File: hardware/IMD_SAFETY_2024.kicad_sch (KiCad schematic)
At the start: 94 parts, among them J1 Main- M80-5300842, K2 TE AXICOM IM07DTS, Q1 2N7002, Q2 2N7002, SW1 Push Button, U1 LM393, U10 74HCS08, U13 74HC74, U14 LM393, U15 LM393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

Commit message: OxDRC state, 2.1.0 ready to review, change connector to vertical, and R-Reset node slightly
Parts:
- J1: value Main- M80-5300842 -> Main- M80-5000842; footprint Samacsys:M80-53008YY -> footprints:M80-50008YY_2
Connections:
- net RESET: now also C13.1, D8.1 (A1), R22.1, U13.3 (C); no longer J1.4 (Pin_4), R22.2, SW1.2
- new net EXT_RESET: J1.4 (Pin_4), R22.2, SW1.2
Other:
- note added: "'0' WHEN > 3.27V ON RISING OF PWM"
- note added: "Legacy RC Hold, populate only if necessary, otherwise short."
- note removed: "'0' WHEN > 1V ON RISING OF PWM"
- note removed: "DODAĆ TVS, CAP 100nF i 100R"
- note removed: "Jumper option"
- note removed: "Legacy RC Hold, bypass. populate only if necessary"
- moved on the sheet: D1, D3, Q2, R21, SW1

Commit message: 2.1.0 Release, adjust after review
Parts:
- added C22: 100nF, Capacitor_SMD:C_0603_1608Metric, symbol Device:C_Small
- F1: symbol PUTM_EV_IMD_SAFETY_2021-rescue:Fuse-Device -> Device:Polyfuse; Mouser# 667-ERB-RG0R50V -> 576-1206L050/24WR
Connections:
- net +12V: now also C22.1
- net GND: now also C22.2
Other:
- moved on the sheet: C4, C5

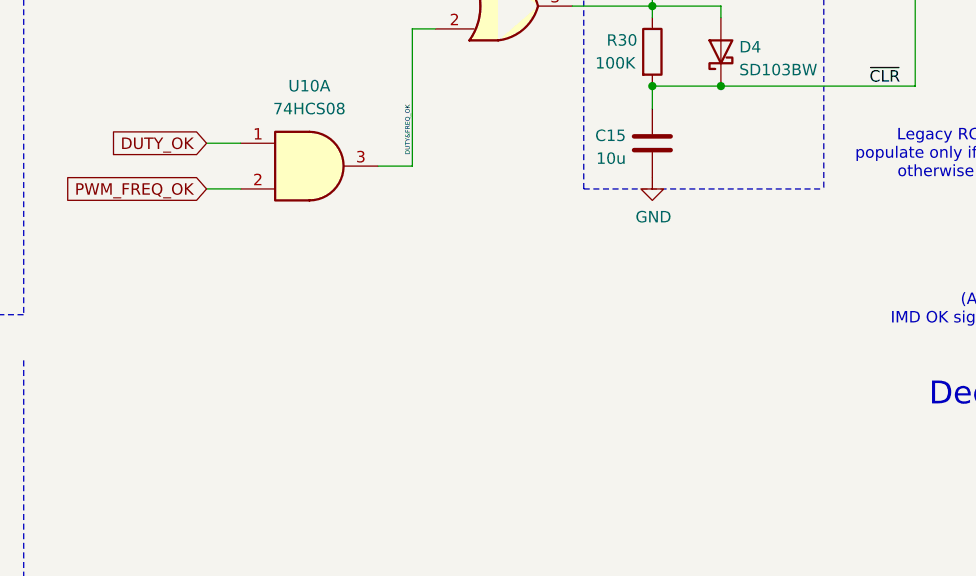
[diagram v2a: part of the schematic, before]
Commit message: Add 0V jumper
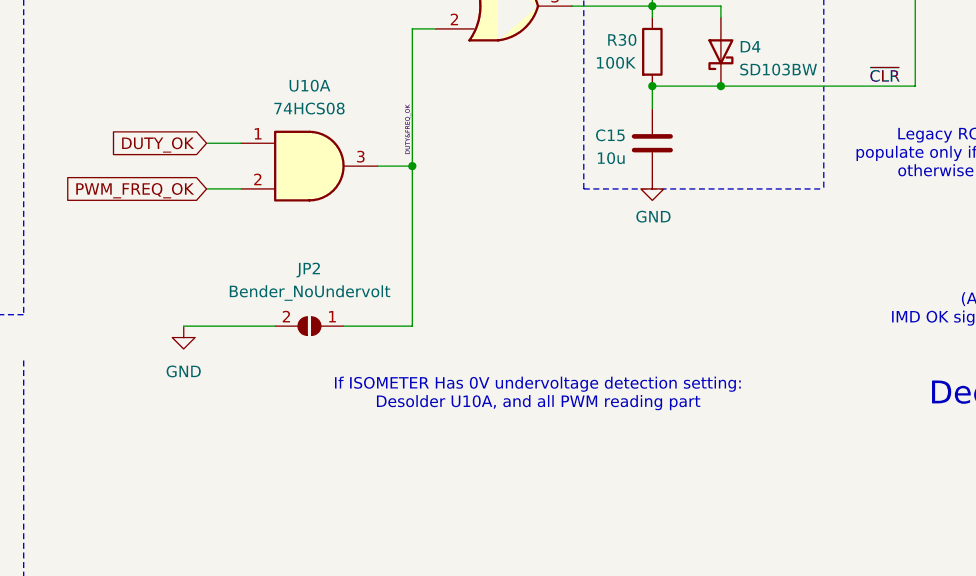
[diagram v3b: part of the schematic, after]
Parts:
- added JP2: Bender_NoUndervolt, Jumper:SolderJumper-2_P1.3mm_Open_Pad1.0x1.5mm, symbol Jumper:SolderJumper_2_Open
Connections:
- net DUTY&FREQ_OK: now also JP2.1 (A)
- net GND: now also JP2.2 (B)
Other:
- note added: "If ISOMETER Has 0V undervoltage detection setting: Desolder U10A, and all PWM reading part"
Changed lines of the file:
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@@
 	)
 	(junction
+		(at 240.03 166.37)
+		(diameter 0)
+		(color 0 0 0 0)
+	)
+	(junction
 		(at 359.41 146.05)
 		(diameter 0)
@@
 		)
 	)
+	(wire
+		(pts
+			(xy 240.03 166.37) (xy 240.03 184.15)
+		)
+		(stroke
+			(width 0)
+			(type default)
+		)
+	)
 	(polyline
 		(pts
@@
 		)
 	)
+	(wire
+		(pts
+			(xy 224.79 184.15) (xy 214.63 184.15)
+		)
+		(stroke
+			(width 0)
+			(type default)
+		)
+	)
 	(polyline
 		(pts
@@
 	(wire
 		(pts
+			(xy 240.03 184.15) (xy 232.41 184.15)
+		)
+		(stroke
+			(width 0)
+			(type default)
+		)
+	)
+	(wire
+		(pts
 			(xy 227.33 96.52) (xy 227.33 97.79)
 		)
@@
 		)
 	)
+	(text "If ISOMETER Has 0V undervoltage detection setting:\nDesolder U10A, and all PWM reading part"
+		(exclude_from_sim no)
+		(at 254 191.77 0)
+		(effects
+			(font
+				(size 1.27 1.27)
+			)
+		)
+	)
 	(text "AND functionality\nby Open Drain outputs"
 		(exclude_from_sim no)
@@
 	)
 	(symbol
+		(lib_id "Jumper:SolderJumper_2_Open")
+		(at 228.6 184.15 0)
+		(mirror y)
+		(unit 1)
+		(exclude_from_sim no)
+		(in_bom yes)
+		(on_board yes)
+		(dnp no)
+		(fields_autoplaced yes)
+		(property "Reference" "JP2"
+			(at 228.6 177.8 0)
+			(effects
+				(font
+					(size 1.27 1.27)
+				)
+			)
+		)
+		(property "Value" "Bender_NoUndervolt"
+			(at 228.6 180.34 0)
+			(effects
+				(font
+					(size 1.27 1.27)
+				)
+			)
+		)
+		(property "Footprint" "Jumper:SolderJumper-2_P1.3mm_Open_Pad1.0x1.5mm"
+			(at 228.6 184.15 0)
+			(effects
+				(font
+					(size 1.27 1.27)
+				)
+				(hide yes)
+			)
+		)
+		(property "Datasheet" "~"
+			(at 228.6 184.15 0)
+			(effects
+				(font
+					(size 1.27 1.27)
+				)
+				(hide yes)
+			)
+		)
+		(property "Description" "Solder Jumper, 2-pole, open"
+			(at 228.6 184.15 0)
+			(effects
+				(font
+					(size 1.27 1.27)
+				)
+				(hide yes)
+			)
+		)
+		(property "Mouser#" ""
+			(at 228.6 184.15 0)
+			(effects
+				(font
+					(size 1.27 1.27)
+				)
+				(hide yes)
+			)
+		)
+		(property "TME#" ""
+			(at 228.6 184.15 0)
+			(effects
+				(font
+					(size 1.27 1.27)
+				)
+				(hide yes)
+			)
+		)
+		(pin "1"
+		)
+		(pin "2"
+		)
+		(instances
+			(project "IMD_SAFETY_2024"
+				(path "/b652b05a-4e3d-4ad1-b032-18886abe7d45"
+					(reference "JP2")
+					(unit 1)
+				)
+			)
+		)
+	)
+	(symbol
 		(lib_id "PUTM_EV_IMD_SAFETY_2021-rescue:+5V-power")
 		(at 340.36 26.67 0)
@@
 					(unit 1)
 				)
+			)
+		)
+	)
+	(symbol
+		(lib_id "power:GND")
+		(at 214.63 184.15 0)
+		(mirror y)
+		(unit 1)
+		(exclude_from_sim no)
+		(in_bom yes)
+		(on_board yes)
+		(dnp no)
+		(fields_autoplaced yes)
+		(property "Reference" "#PWR076"
+			(at 214.63 190.5 0)
+			(effects
+				(font
+					(size 1.27 1.27)
+				)
+				(hide yes)
+			)
+		)
+		(property "Value" "GND"
+			(at 214.63 189.23 0)
+			(effects
+				(font
+					(size 1.27 1.27)
+				)
+			)
+		)
+		(property "Footprint" ""
+			(at 214.63 184.15 0)
+			(effects
+				(font
+					(size 1.27 1.27)
+				)
+				(hide yes)
+			)
+		)
+		(property "Datasheet" ""
+			(at 214.63 184.15 0)
+			(effects
+				(font
+					(size 1.27 1.27)
+				)
+				(hide yes)
+			)
+		)
+		(property "Description" "Power symbol creates a global label with name \"GND\" , ground"
+			(at 214.63 184.15 0)
+			(effects
+				(font
+					(size 1.27 1.27)
+				)
+				(hide yes)
+			)
+		)
+		(pin "1"
+		)
+		(instances
+			(project "IMD_SAFETY_2024"
+				(path "/b652b05a-4e3d-4ad1-b032-18886abe7d45"
+					(reference "#PWR076")
+					(unit 1)
+				)

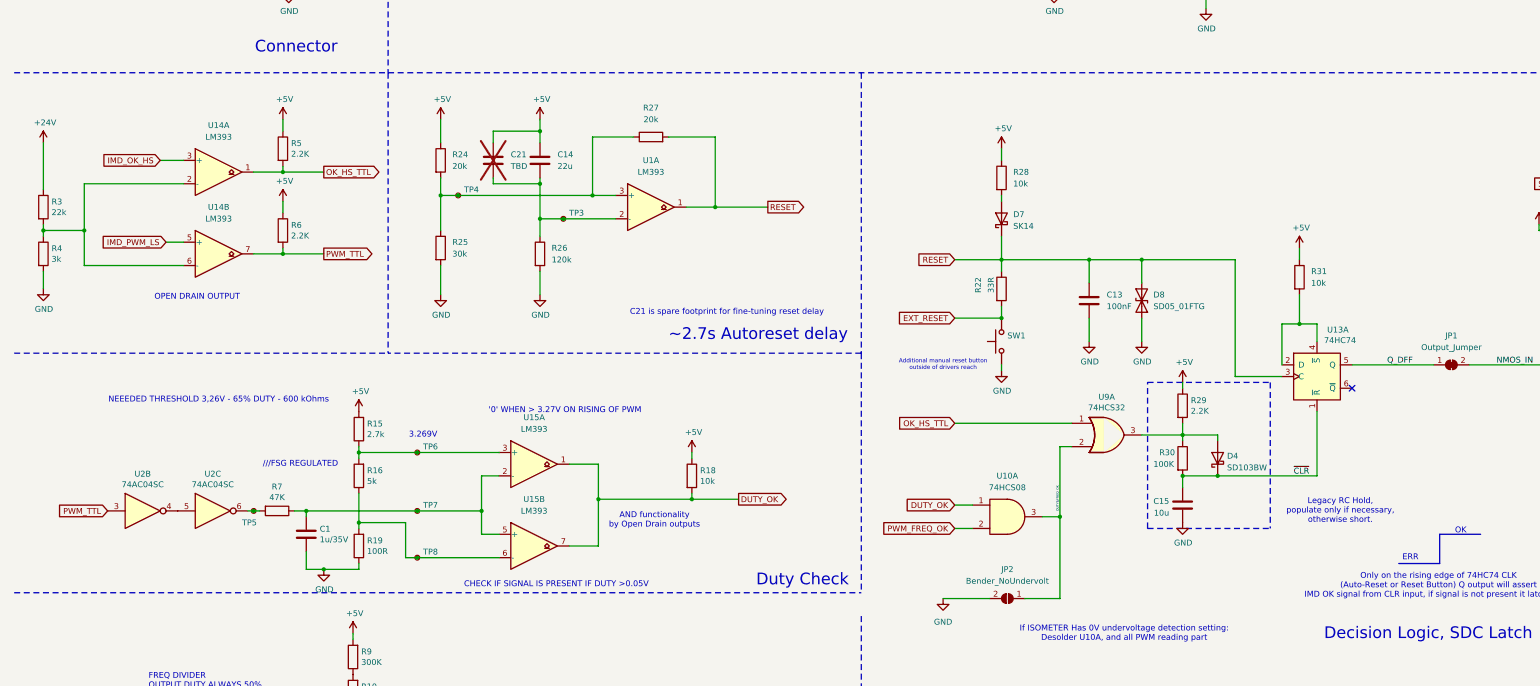
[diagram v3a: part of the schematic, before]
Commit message: Add input stage LM393 comment
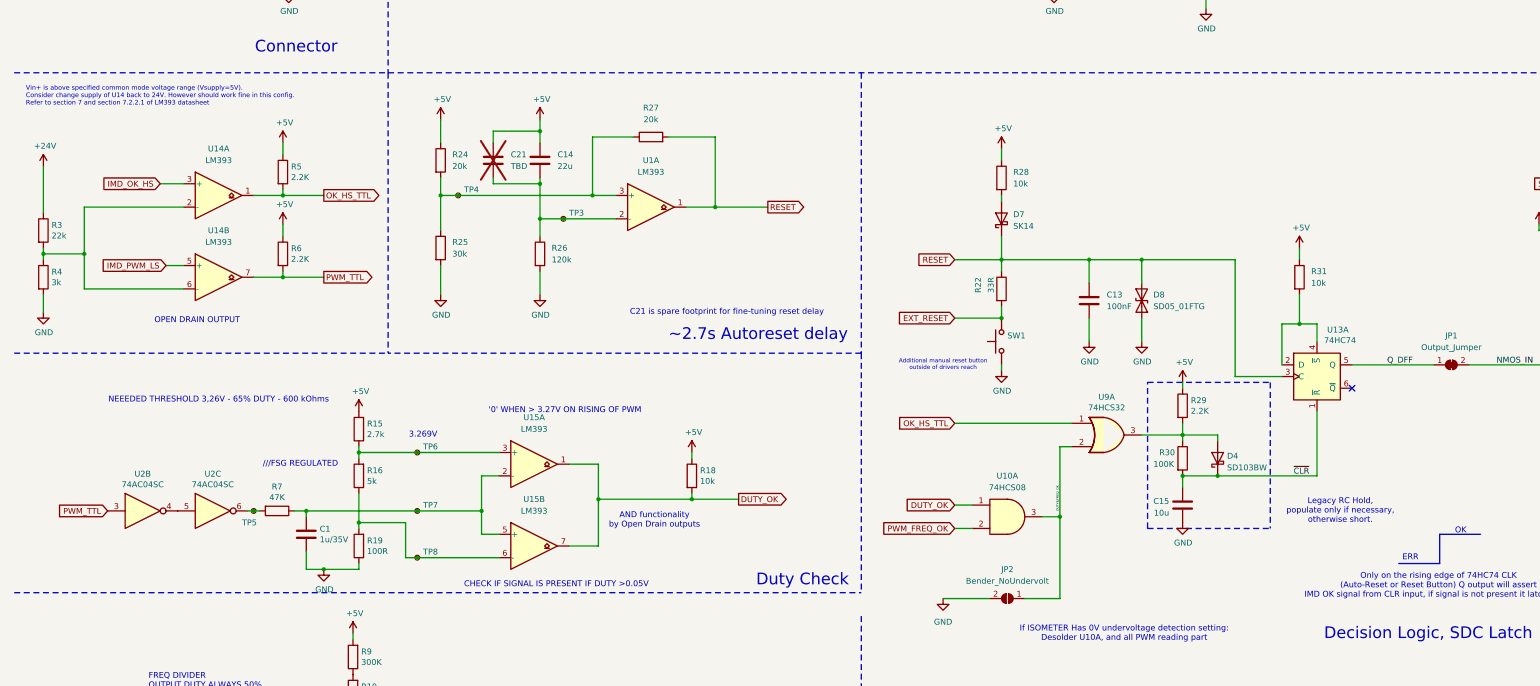
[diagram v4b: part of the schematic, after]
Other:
- note added: "Vin+ is above specified common mode voltage range (Vsupply=5V). Consider change supply of U14 back to 24V. However should work fine in this config. Refer to section 7 and section 7.2.2.1 of LM393 datasheet"
- moved on the sheet: R3, R4, R5, R6, U14A, U14B
